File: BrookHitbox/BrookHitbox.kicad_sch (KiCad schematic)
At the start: 16 parts

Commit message: scrapwork script for calculating coordinates
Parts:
- renumbered U1 to BrookConnection1, SW_CIRCLE to SW_CIRCLE1, SW_DOWN to SW_DOWN1, SW_LEFT to SW_LEFT1, SW_PSXBOX to SW_PSXBOX1, SW_RIGHT to SW_RIGHT1, SW_SELECT to SW_SELECT1, SW_SQUARE to SW_SQUARE1, SW_START to SW_START1, SW_TRIANGLE to SW_TRIANGLE1, SW_UP to SW_UP1, SW_X to SW_X1

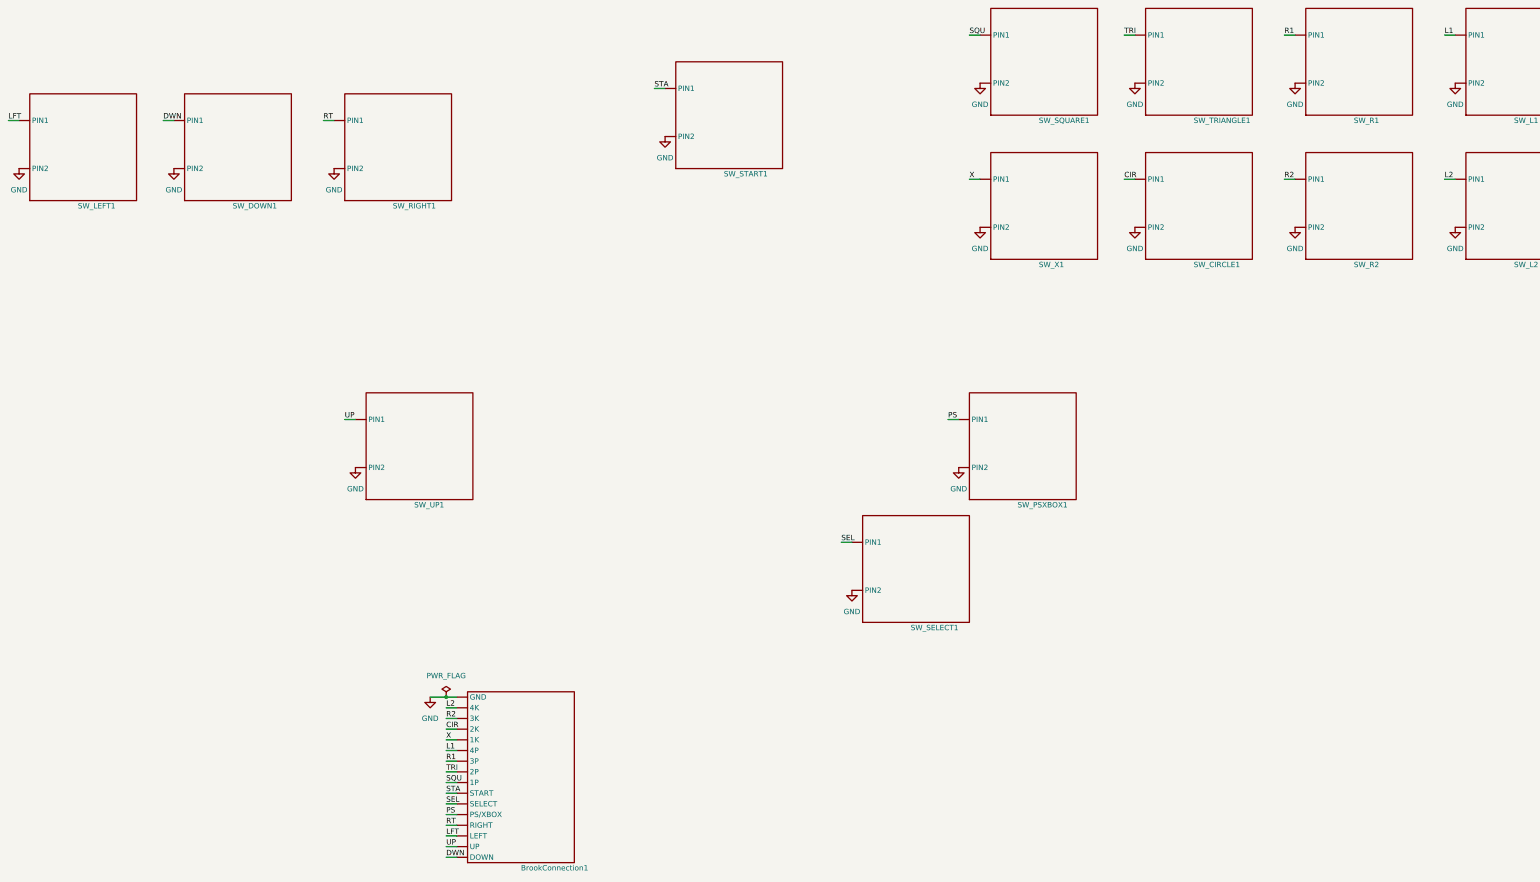
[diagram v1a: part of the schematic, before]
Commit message: fix ERC errors, fix ratsnest not showing
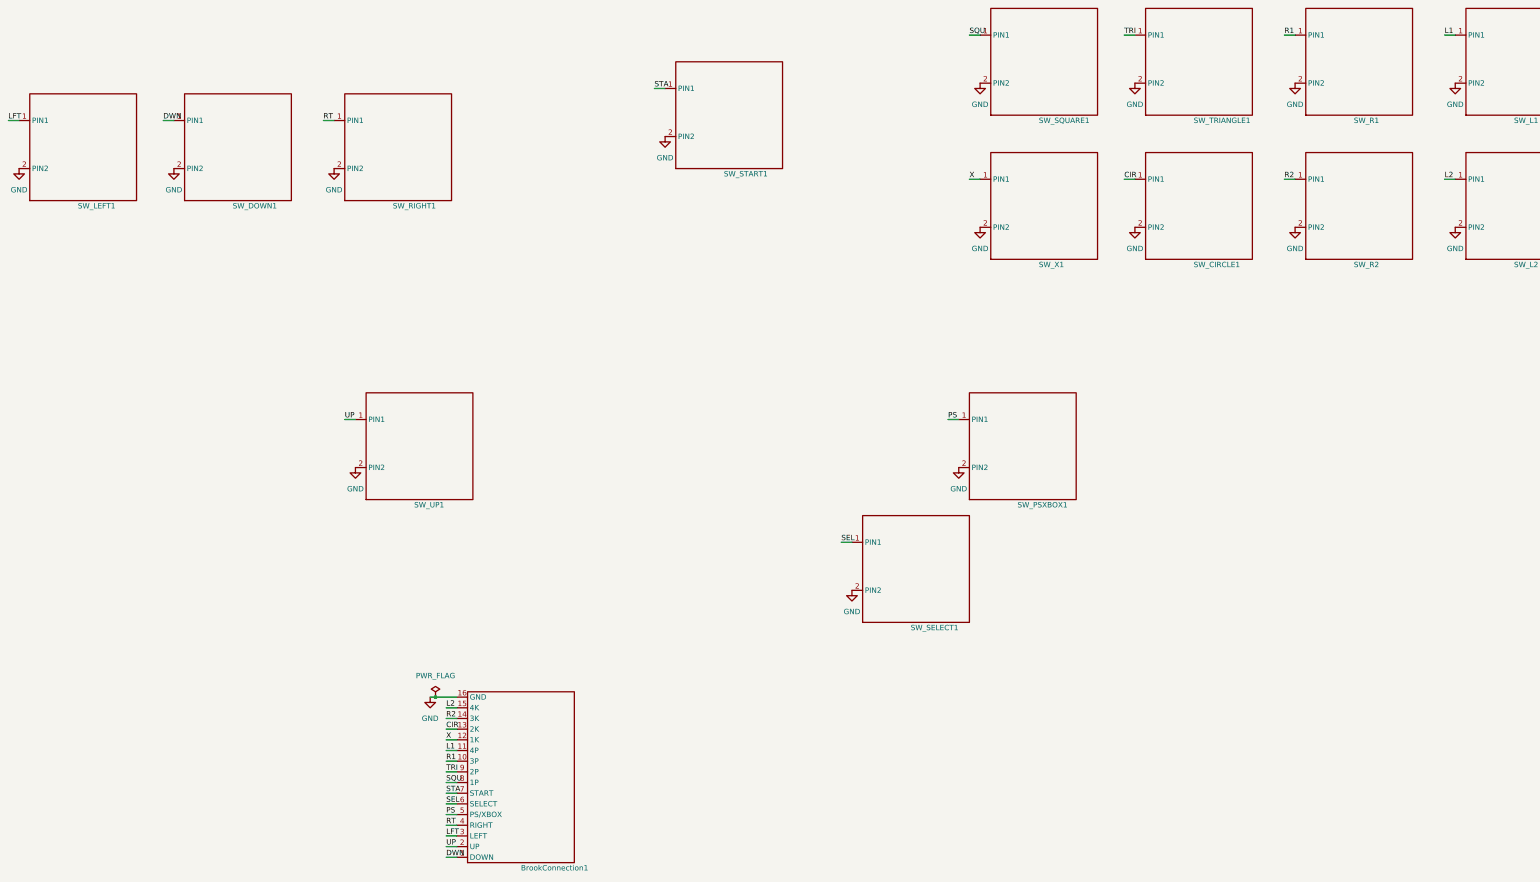
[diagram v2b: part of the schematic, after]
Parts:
- BrookConnection1: footprint (none) -> BrookHitboxFootprints:BrookConn16
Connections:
- net CIR: now also BrookConnection1.13 (2K), SW_CIRCLE1.1 (PIN1); no longer BrookConnection1. (UP), SW_CIRCLE1. (PIN2)
- net DWN: now also BrookConnection1.1 (DOWN), SW_DOWN1.1 (PIN1); no longer BrookConnection1. (UP), SW_DOWN1. (PIN2)
- net GND: now also BrookConnection1.16 (GND), SW_CIRCLE1.2 (PIN2), SW_DOWN1.2 (PIN2), SW_L1.2 (PIN2), SW_L2.2 (PIN2), SW_LEFT1.2 (PIN2), SW_PSXBOX1.2 (PIN2), SW_R1.2 (PIN2), SW_R2.2 (PIN2), SW_RIGHT1.2 (PIN2), SW_SELECT1.2 (PIN2), SW_SQUARE1.2 (PIN2), SW_START1.2 (PIN2), SW_TRIANGLE1.2 (PIN2), SW_UP1.2 (PIN2), SW_X1.2 (PIN2); no longer BrookConnection1. (UP), SW_CIRCLE1. (PIN2), SW_DOWN1. (PIN2), SW_L1. (PIN2), SW_L2. (PIN2), SW_LEFT1. (PIN2), SW_PSXBOX1. (PIN2), SW_R1. (PIN2), SW_R2. (PIN2), SW_RIGHT1. (PIN2), SW_SELECT1. (PIN2), SW_SQUARE1. (PIN2), SW_START1. (PIN2), SW_TRIANGLE1. (PIN2), SW_UP1. (PIN2), SW_X1. (PIN2)
- net L1: now also BrookConnection1.11 (4P), SW_L1.1 (PIN1); no longer BrookConnection1. (UP), SW_L1. (PIN2)
- net L2: now also BrookConnection1.15 (4K), SW_L2.1 (PIN1); no longer BrookConnection1. (UP), SW_L2. (PIN2)
- net LFT: now also BrookConnection1.3 (LEFT), SW_LEFT1.1 (PIN1); no longer BrookConnection1. (UP), SW_LEFT1. (PIN2)
- net PS: now also BrookConnection1.5 (PS/XBOX), SW_PSXBOX1.1 (PIN1); no longer BrookConnection1. (UP), SW_PSXBOX1. (PIN2)
- net R1: now also BrookConnection1.10 (3P), SW_R1.1 (PIN1); no longer BrookConnection1. (UP), SW_R1. (PIN2)
- net R2: now also BrookConnection1.14 (3K), SW_R2.1 (PIN1); no longer BrookConnection1. (UP), SW_R2. (PIN2)
- net RT: now also BrookConnection1.4 (RIGHT), SW_RIGHT1.1 (PIN1); no longer BrookConnection1. (UP), SW_RIGHT1. (PIN2)
- net SEL: now also BrookConnection1.6 (SELECT), SW_SELECT1.1 (PIN1); no longer BrookConnection1. (UP), SW_SELECT1. (PIN2)
- net SQU: now also BrookConnection1.8 (1P), SW_SQUARE1.1 (PIN1); no longer BrookConnection1. (UP), SW_SQUARE1. (PIN2)
- net STA: now also BrookConnection1.7 (START), SW_START1.1 (PIN1); no longer BrookConnection1. (UP), SW_START1. (PIN2)
- net TRI: now also BrookConnection1.9 (2P), SW_TRIANGLE1.1 (PIN1); no longer BrookConnection1. (UP), SW_TRIANGLE1. (PIN2)
- net UP: now also BrookConnection1.2 (UP), SW_UP1.1 (PIN1); no longer BrookConnection1. (UP), SW_UP1. (PIN2)
- net X: now also BrookConnection1.12 (1K), SW_X1.1 (PIN1); no longer BrookConnection1. (UP), SW_X1. (PIN2)
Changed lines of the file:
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@@
 (kicad_sch (version 20230121) (generator eeschema)
   (paper "A3")
-  (junction (at 132.08 186.69) (diameter 0) (color 0 0 0 0)
+  (junction (at 129.54 186.69) (diameter 0) (color 0 0 0 0)
   )
   (wire (pts (xy 132.08 209.55) (xy 134.62 209.55))
@@
     (stroke (width 0) (type default))
   )
-  (wire (pts (xy 132.08 186.69) (xy 134.62 186.69))
-    (stroke (width 0) (type default))
-  )
   (wire (pts (xy 132.08 207.01) (xy 134.62 207.01))
     (stroke (width 0) (type default))
@@
     (stroke (width 0) (type default))
   )
+  (wire (pts (xy 129.54 186.69) (xy 134.62 186.69))
+    (stroke (width 0) (type default))
+  )
   (wire (pts (xy 107.95 120.65) (xy 110.49 120.65))
     (stroke (width 0) (type default))
@@
     (stroke (width 0) (type default))
   )
-  (wire (pts (xy 128.27 186.69) (xy 132.08 186.69))
+  (wire (pts (xy 128.27 186.69) (xy 129.54 186.69))
     (stroke (width 0) (type default))
   )
@@
       (effects (font (size 1.27 1.27)) hide)
     )
-    (pin "")
-    (pin "")
+    (pin "1")
+    (pin "2")
     (instances
       (project "BrookHitbox"
@@
       (effects (font (size 1.27 1.27)) hide)
     )
-    (pin "")
-    (pin "")
+    (pin "1")
+    (pin "2")
     (instances
       (project "BrookHitbox"
@@
       (effects (font (size 1.27 1.27)))
     )
-    (property "Footprint" "" (at 137.16 226.06 0)
+    (property "Footprint" "BrookHitboxFootprints:BrookConn16" (at 137.16 226.06 0)
       (effects (font (size 1.27 1.27)) hide)
     )
@@
       (effects (font (size 1.27 1.27)) hide)
     )
-    (pin "")
-    (pin "")
-    (pin "")
-    (pin "")
-    (pin "")
-    (pin "")
-    (pin "")
-    (pin "")
-    (pin "")
-    (pin "")
-    (pin "")
-    (pin "")
-    (pin "")
-    (pin "")
-    (pin "")
-    (pin "")
+    (pin "1")
+    (pin "10")
+    (pin "11")
+    (pin "12")
+    (pin "13")
+    (pin "14")
+    (pin "15")
+    (pin "16")
+    (pin "2")
+    (pin "3")
+    (pin "4")
+    (pin "5")
+    (pin "6")
+    (pin "7")
+    (pin "8")
+    (pin "9")
     (instances
       (project "BrookHitbox"
@@
       (effects (font (size 1.27 1.27)) hide)
     )
-    (pin "")
-    (pin "")
+    (pin "1")
+    (pin "2")
     (instances
       (project "BrookHitbox"
@@
       (effects (font (size 1.27 1.27)) hide)
     )
-    (pin "")
-    (pin "")
+    (pin "1")
+    (pin "2")
     (instances
       (project "BrookHitbox"
@@
       (effects (font (size 1.27 1.27)) hide)
     )
-    (pin "")
-    (pin "")
+    (pin "1")
+    (pin "2")
     (instances
       (project "BrookHitbox"
@@
       (effects (font (size 1.27 1.27)) hide)
     )
-    (pin "")
-    (pin "")
+    (pin "1")
+    (pin "2")
     (instances
       (project "BrookHitbox"
@@
       (effects (font (size 1.27 1.27)) hide)
     )
-    (pin "")
-    (pin "")
+    (pin "1")
+    (pin "2")
     (instances
       (project "BrookHitbox"
@@
       (effects (font (size 1.27 1.27)) hide)
     )
-    (pin "")
-    (pin "")
+    (pin "1")
+    (pin "2")
     (instances
       (project "BrookHitbox"
@@
     )
   )
-  (symbol (lib_id "power:PWR_FLAG") (at 132.08 186.69 0) (unit 1)
-    (in_bom yes) (on_board yes) (dnp no) (fields_autoplaced)
-    (property "Reference" "#FLG01" (at 132.08 184.785 0)
-      (effects (font (size 1.27 1.27)) hide)
-    )
-    (property "Value" "PWR_FLAG" (at 132.08 181.61 0)
-      (effects (font (size 1.27 1.27)))
-    )
-    (property "Footprint" "" (at 132.08 186.69 0)
-      (effects (font (size 1.27 1.27)) hide)
-    )
-    (property "Datasheet" "~" (at 132.08 186.69 0)
+  (symbol (lib_id "power:PWR_FLAG") (at 129.54 186.69 0) (unit 1)
+    (in_bom yes) (on_board yes) (dnp no) (fields_autoplaced)
+    (property "Reference" "#FLG01" (at 129.54 184.785 0)
+      (effects (font (size 1.27 1.27)) hide)
+    )
+    (property "Value" "PWR_FLAG" (at 129.54 181.61 0)
+      (effects (font (size 1.27 1.27)))
+    )
+    (property "Footprint" "" (at 129.54 186.69 0)
+      (effects (font (size 1.27 1.27)) hide)
+    )
+    (property "Datasheet" "~" (at 129.54 186.69 0)
       (effects (font (size 1.27 1.27)) hide)
     )
@@
       (effects (font (size 1.27 1.27)) hide)
     )
-    (pin "")
-    (pin "")
+    (pin "1")
+    (pin "2")
     (instances
       (project "BrookHitbox"
@@
       (effects (font (size 1.27 1.27)) hide)
     )
-    (pin "")
-    (pin "")
+    (pin "1")
+    (pin "2")
     (instances
       (project "BrookHitbox"
@@
       (effects (font (size 1.27 1.27)) hide)
     )
-    (pin "")
-    (pin "")
+    (pin "1")
+    (pin "2")
     (instances
       (project "BrookHitbox"
@@
       (effects (font (size 1.27 1.27)) hide)
     )
-    (pin "")
-    (pin "")
+    (pin "1")
+    (pin "2")
     (instances
       (project "BrookHitbox"
@@
       (effects (font (size 1.27 1.27)) hide)
     )
-    (pin "")
-    (pin "")
+    (pin "1")
+    (pin "2")
     (instances
       (project "BrookHitbox"
@@
       (effects (font (size 1.27 1.27)) hide)
     )
-    (pin "")
-    (pin "")
+    (pin "1")
+    (pin "2")
     (instances
       (project "BrookHitbox"
@@
       (effects (font (size 1.27 1.27)) hide)
     )
-    (pin "")
-    (pin "")
-    (instances
-      (project "BrookHitbox"
+    (pin "1")
+    (pin "2")
+    (instances
+      (project "BrookHitbox"

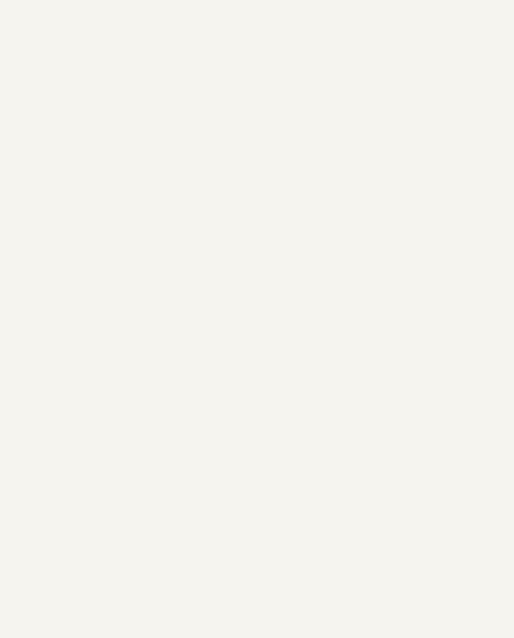
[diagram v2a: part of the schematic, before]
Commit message: add mounting holes
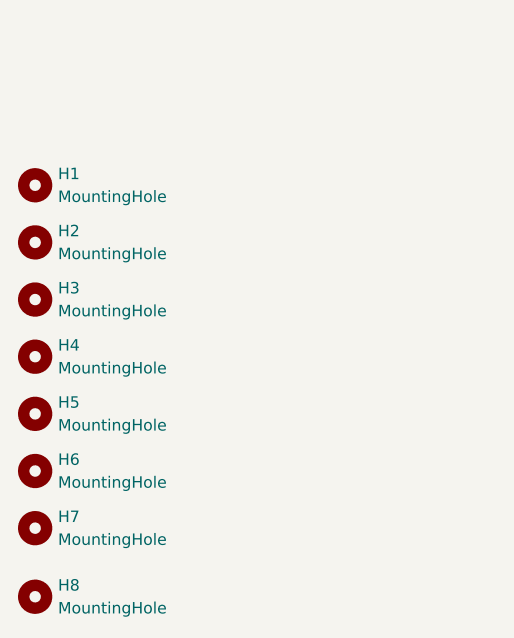
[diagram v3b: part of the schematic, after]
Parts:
- added H1, H2, H3, H4, H5, H6, H7, H8: MountingHole, MountingHole:MountingHole_2.2mm_M2, symbol Mechanical:MountingHole
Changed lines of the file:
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@@
+    )
+  )
+  (symbol (lib_id "Mechanical:MountingHole") (at 16.51 213.36 0) (unit 1)
+    (in_bom yes) (on_board yes) (dnp no) (fields_autoplaced)
+    (property "Reference" "H5" (at 19.05 212.09 0)
+      (effects (font (size 1.27 1.27)) (justify left))
+    )
+    (property "Value" "MountingHole" (at 19.05 214.63 0)
+      (effects (font (size 1.27 1.27)) (justify left))
+    )
+    (property "Footprint" "MountingHole:MountingHole_2.2mm_M2" (at 16.51 213.36 0)
+      (effects (font (size 1.27 1.27)) hide)
+    )
+    (property "Datasheet" "~" (at 16.51 213.36 0)
+      (effects (font (size 1.27 1.27)) hide)
+    )
+    (instances
+      (project "BrookHitbox"
+        (path "/8a682108-57a0-4e08-bf48-a8e61ef9e3ef"
+          (reference "H5") (unit 1)
+        )
+      )
+    )
+  )
+  (symbol (lib_id "Mechanical:MountingHole") (at 16.51 207.01 0) (unit 1)
+    (in_bom yes) (on_board yes) (dnp no) (fields_autoplaced)
+    (property "Reference" "H4" (at 19.05 205.74 0)
+      (effects (font (size 1.27 1.27)) (justify left))
+    )
+    (property "Value" "MountingHole" (at 19.05 208.28 0)
+      (effects (font (size 1.27 1.27)) (justify left))
+    )
+    (property "Footprint" "MountingHole:MountingHole_2.2mm_M2" (at 16.51 207.01 0)
+      (effects (font (size 1.27 1.27)) hide)
+    )
+    (property "Datasheet" "~" (at 16.51 207.01 0)
+      (effects (font (size 1.27 1.27)) hide)
+    )
+    (instances
+      (project "BrookHitbox"
+        (path "/8a682108-57a0-4e08-bf48-a8e61ef9e3ef"
+          (reference "H4") (unit 1)
+        )
+      )
+    )
+  )
+  (symbol (lib_id "Mechanical:MountingHole") (at 16.51 187.96 0) (unit 1)
+    (in_bom yes) (on_board yes) (dnp no) (fields_autoplaced)
+    (property "Reference" "H1" (at 19.05 186.69 0)
+      (effects (font (size 1.27 1.27)) (justify left))
+    )
+    (property "Value" "MountingHole" (at 19.05 189.23 0)
+      (effects (font (size 1.27 1.27)) (justify left))
+    )
+    (property "Footprint" "MountingHole:MountingHole_2.2mm_M2" (at 16.51 187.96 0)
+      (effects (font (size 1.27 1.27)) hide)
+    )
+    (property "Datasheet" "~" (at 16.51 187.96 0)
+      (effects (font (size 1.27 1.27)) hide)
+    )
+    (instances
+      (project "BrookHitbox"
+        (path "/8a682108-57a0-4e08-bf48-a8e61ef9e3ef"
+          (reference "H1") (unit 1)
+        )
+      )
     )
   )
@@
     )
   )
+  (symbol (lib_id "Mechanical:MountingHole") (at 16.51 194.31 0) (unit 1)
+    (in_bom yes) (on_board yes) (dnp no) (fields_autoplaced)
+    (property "Reference" "H2" (at 19.05 193.04 0)
+      (effects (font (size 1.27 1.27)) (justify left))
+    )
+    (property "Value" "MountingHole" (at 19.05 195.58 0)
+      (effects (font (size 1.27 1.27)) (justify left))
+    )
+    (property "Footprint" "MountingHole:MountingHole_2.2mm_M2" (at 16.51 194.31 0)
+      (effects (font (size 1.27 1.27)) hide)
+    )
+    (property "Datasheet" "~" (at 16.51 194.31 0)
+      (effects (font (size 1.27 1.27)) hide)
+    )
+    (instances
+      (project "BrookHitbox"
+        (path "/8a682108-57a0-4e08-bf48-a8e61ef9e3ef"
+          (reference "H2") (unit 1)
+        )
+      )
+    )
+  )
   (symbol (lib_id "power:GND") (at 30.48 60.96 0) (unit 1)
     (in_bom yes) (on_board yes) (dnp no) (fields_autoplaced)
@@
     )
   )
+  (symbol (lib_id "Mechanical:MountingHole") (at 16.51 219.71 0) (unit 1)
+    (in_bom yes) (on_board yes) (dnp no) (fields_autoplaced)
+    (property "Reference" "H6" (at 19.05 218.44 0)
+      (effects (font (size 1.27 1.27)) (justify left))
+    )
+    (property "Value" "MountingHole" (at 19.05 220.98 0)
+      (effects (font (size 1.27 1.27)) (justify left))
+    )
+    (property "Footprint" "MountingHole:MountingHole_2.2mm_M2" (at 16.51 219.71 0)
+      (effects (font (size 1.27 1.27)) hide)
+    )
+    (property "Datasheet" "~" (at 16.51 219.71 0)
+      (effects (font (size 1.27 1.27)) hide)
+    )
+    (instances
+      (project "BrookHitbox"
+        (path "/8a682108-57a0-4e08-bf48-a8e61ef9e3ef"
+          (reference "H6") (unit 1)
+        )
+      )
+    )
+  )
   (symbol (lib_id "BrookHitboxSymbols:MX-SW") (at 298.45 82.55 0) (unit 1)
     (in_bom yes) (on_board yes) (dnp no)
@@
     )
   )
+  (symbol (lib_id "Mechanical:MountingHole") (at 16.51 233.68 0) (unit 1)
+    (in_bom yes) (on_board yes) (dnp no) (fields_autoplaced)
+    (property "Reference" "H8" (at 19.05 232.41 0)
+      (effects (font (size 1.27 1.27)) (justify left))
+    )
+    (property "Value" "MountingHole" (at 19.05 234.95 0)
+      (effects (font (size 1.27 1.27)) (justify left))
+    )
+    (property "Footprint" "MountingHole:MountingHole_2.2mm_M2" (at 16.51 233.68 0)
+      (effects (font (size 1.27 1.27)) hide)
+    )
+    (property "Datasheet" "~" (at 16.51 233.68 0)
+      (effects (font (size 1.27 1.27)) hide)
+    )
+    (instances
+      (project "BrookHitbox"
+        (path "/8a682108-57a0-4e08-bf48-a8e61ef9e3ef"
+          (reference "H8") (unit 1)
+        )
+      )
+    )
+  )
+  (symbol (lib_id "Mechanical:MountingHole") (at 16.51 226.06 0) (unit 1)
+    (in_bom yes) (on_board yes) (dnp no) (fields_autoplaced)
+    (property "Reference" "H7" (at 19.05 224.79 0)
+      (effects (font (size 1.27 1.27)) (justify left))
+    )
+    (property "Value" "MountingHole" (at 19.05 227.33 0)
+      (effects (font (size 1.27 1.27)) (justify left))
+    )
+    (property "Footprint" "MountingHole:MountingHole_2.2mm_M2" (at 16.51 226.06 0)
+      (effects (font (size 1.27 1.27)) hide)
+    )
+    (property "Datasheet" "~" (at 16.51 226.06 0)
+      (effects (font (size 1.27 1.27)) hide)
+    )
+    (instances
+      (project "BrookHitbox"
+        (path "/8a682108-57a0-4e08-bf48-a8e61ef9e3ef"
+          (reference "H7") (unit 1)
+        )
+      )
+    )
+  )
   (symbol (lib_id "power:GND") (at 334.01 40.64 0) (unit 1)
     (in_bom yes) (on_board yes) (dnp no) (fields_autoplaced)
@@
         )
       )
+    )
+  )
+  (symbol (lib_id "Mechanical:MountingHole") (at 16.51 200.66 0) (unit 1)
+    (in_bom yes) (on_board yes) (dnp no) (fields_autoplaced)
+    (property "Reference" "H3" (at 19.05 199.39 0)
+      (effects (font (size 1.27 1.27)) (justify left))
+    )
+    (property "Value" "MountingHole" (at 19.05 201.93 0)
+      (effects (font (size 1.27 1.27)) (justify left))
+    )
+    (property "Footprint" "MountingHole:MountingHole_2.2mm_M2" (at 16.51 200.66 0)
+      (effects (font (size 1.27 1.27)) hide)
+    )
+    (property "Datasheet" "~" (at 16.51 200.66 0)
+      (effects (font (size 1.27 1.27)) hide)
+    )
+    (instances
+      (project "BrookHitbox"
+        (path "/8a682108-57a0-4e08-bf48-a8e61ef9e3ef"
+          (reference "H3") (unit 1)
+        )
+      )
